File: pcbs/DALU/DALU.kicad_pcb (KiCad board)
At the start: 4 copper layers, 46 parts, among them J201 Conn_02x20_Odd_Even, U201 74HC245, U202 74HC245, U203 74HC245, U301 74HC138, U401 74HC86, U402 74HC86, U403 74HC86, U404 74HC08, U405 74HC283, U406 74HC283, U407 74HC245, U408 74HC245, U501 74HC00, U502 74HC00, U505 74HC245, U506 74HC245, U601 74HC86, U602 74HC86, U603 74HC245, U701 74HC245, U801 74HC74, U802 74HCT574

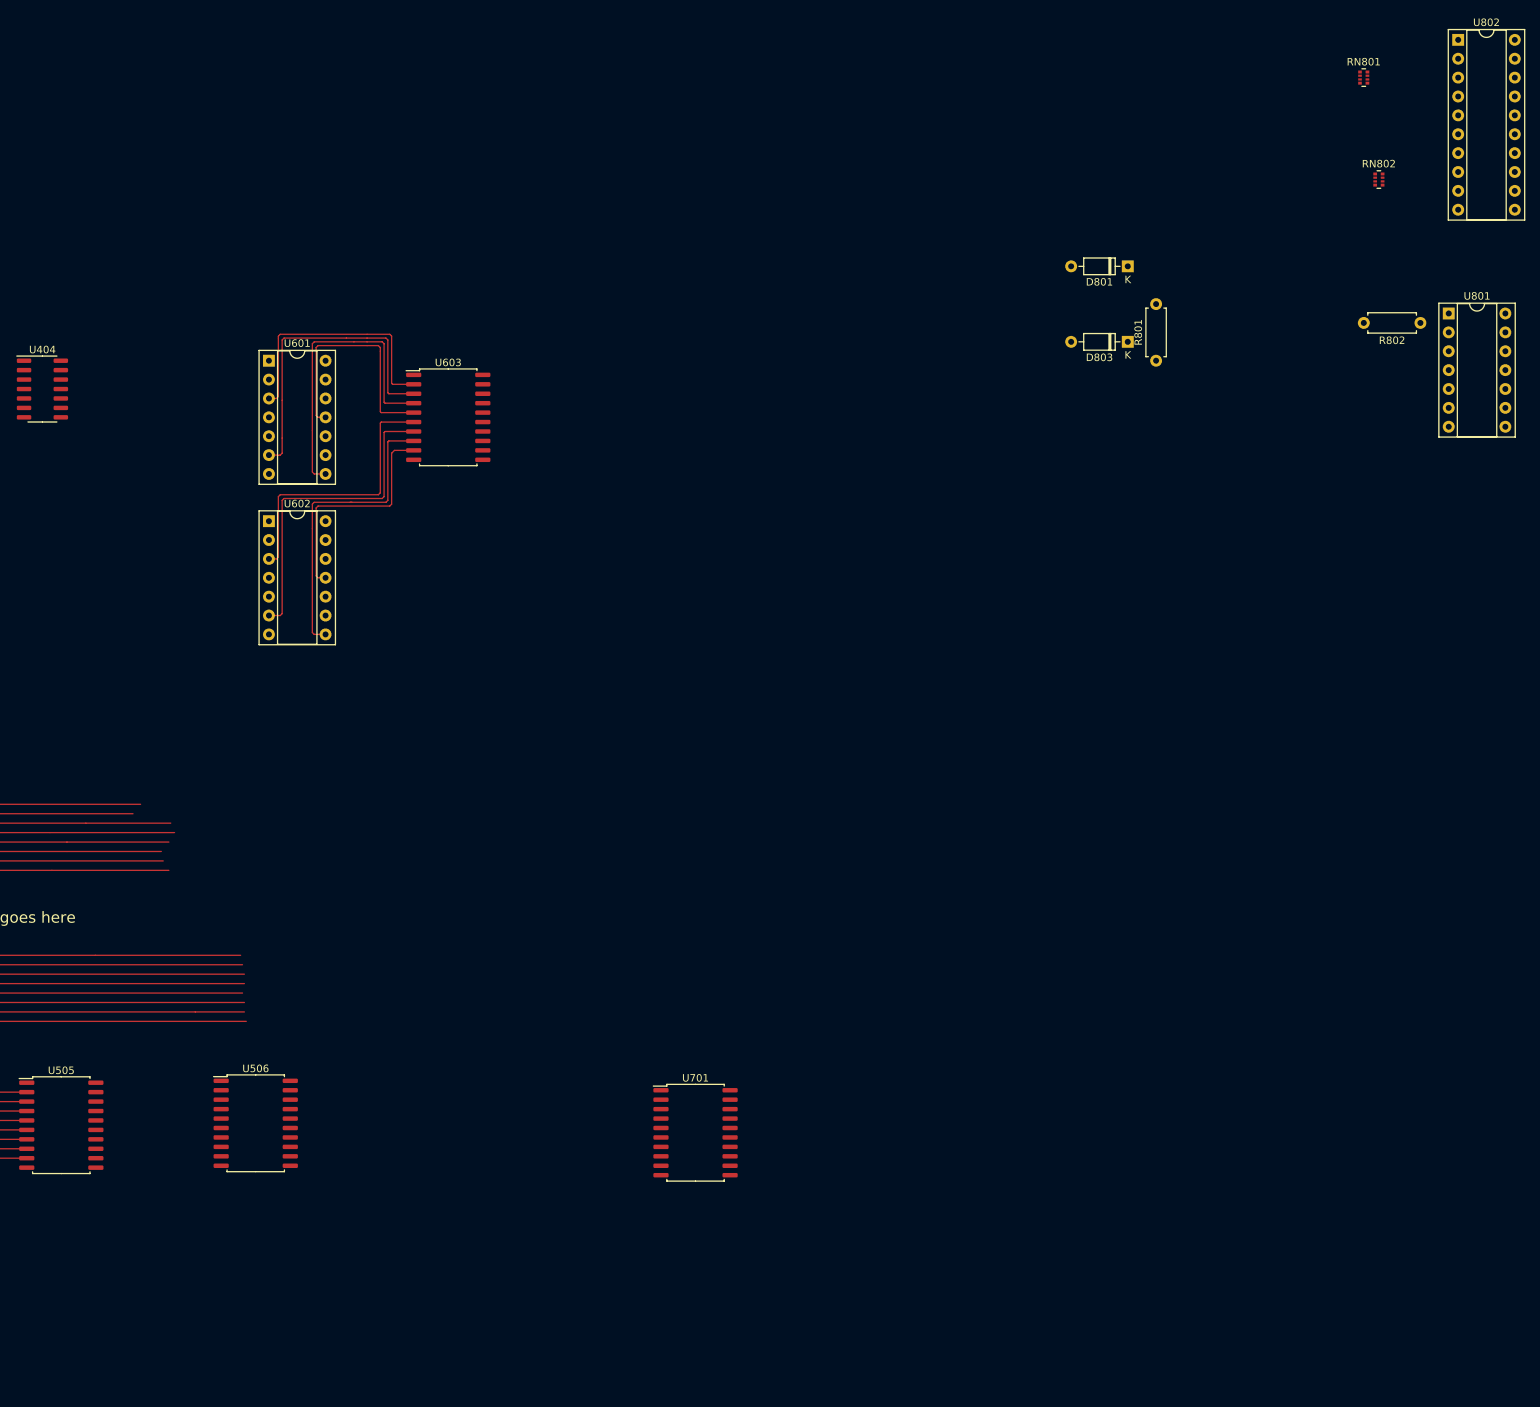
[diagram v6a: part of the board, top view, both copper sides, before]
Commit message: Separate out AND stage
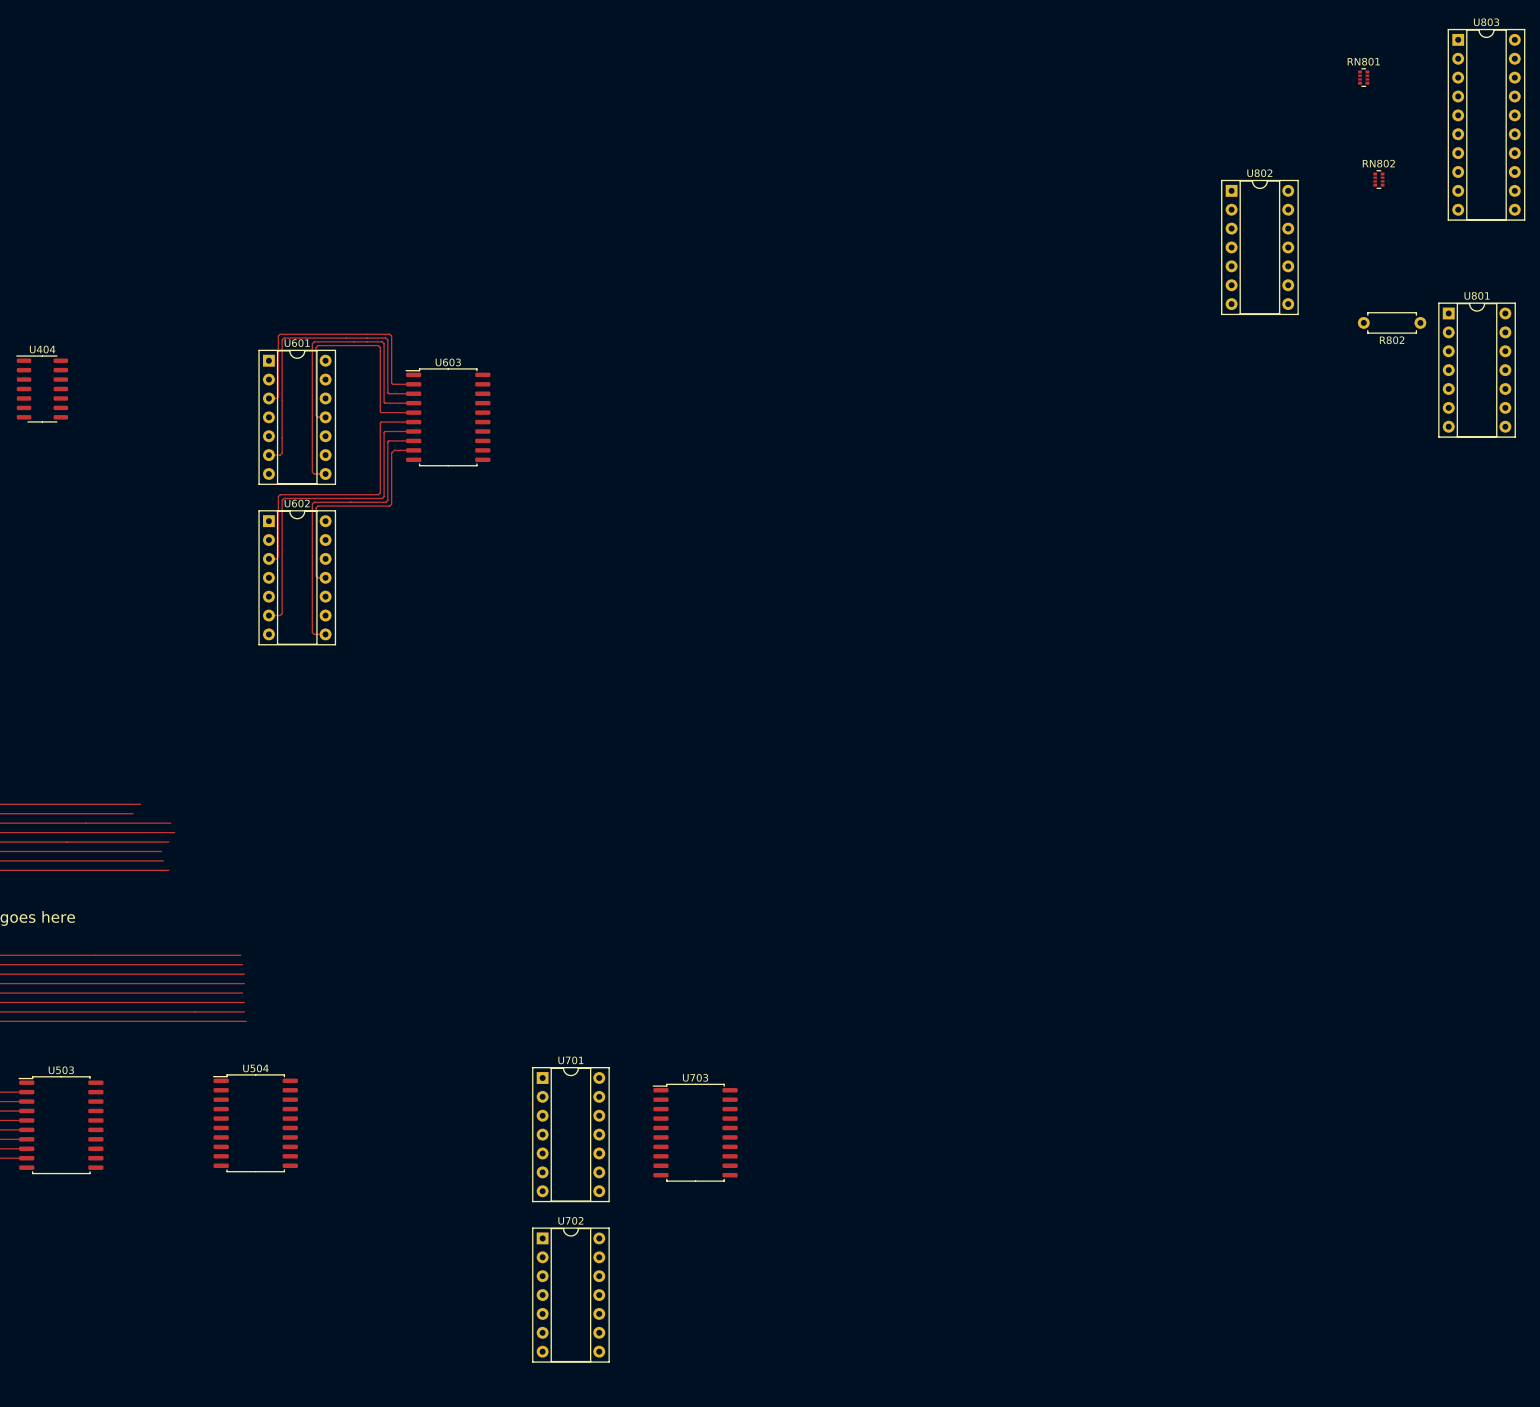
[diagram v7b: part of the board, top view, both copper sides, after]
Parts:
- removed D801, D803: 1N4148, Diode_THT:D_DO-35_SOD27_P7.62mm_Horizontal
- removed R801: 100k, Resistor_THT:R_Axial_DIN0207_L6.3mm_D2.5mm_P7.62mm_Horizontal
- added U701: 74HC32, Package_DIP:DIP-14_W7.62mm_Socket, F.Cu at (175.3, 143.5)
- added U702: 74HC32, Package_DIP:DIP-14_W7.62mm_Socket, F.Cu at (175.3, 165.1)
- added U802: 74HC32, Package_DIP:DIP-14_W7.62mm_Socket, F.Cu at (268.0, 24.1)
- renumbered U505 to U503, U506 to U504, U701 to U703, U802 to U803
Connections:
- U703 pad 2: unconnected-(U701-Pad2) -> /OR/OR0
- U703 pad 3: unconnected-(U701-Pad3) -> /OR/OR1
- U703 pad 4: unconnected-(U701-Pad4) -> /OR/OR2
- U703 pad 5: unconnected-(U701-Pad5) -> /OR/OR3
- U703 pad 6: unconnected-(U701-Pad6) -> /OR/OR4
- U703 pad 7: unconnected-(U701-Pad7) -> /OR/OR5
- U703 pad 8: unconnected-(U701-Pad8) -> /OR/OR6
- U703 pad 9: unconnected-(U701-Pad9) -> /OR/OR7

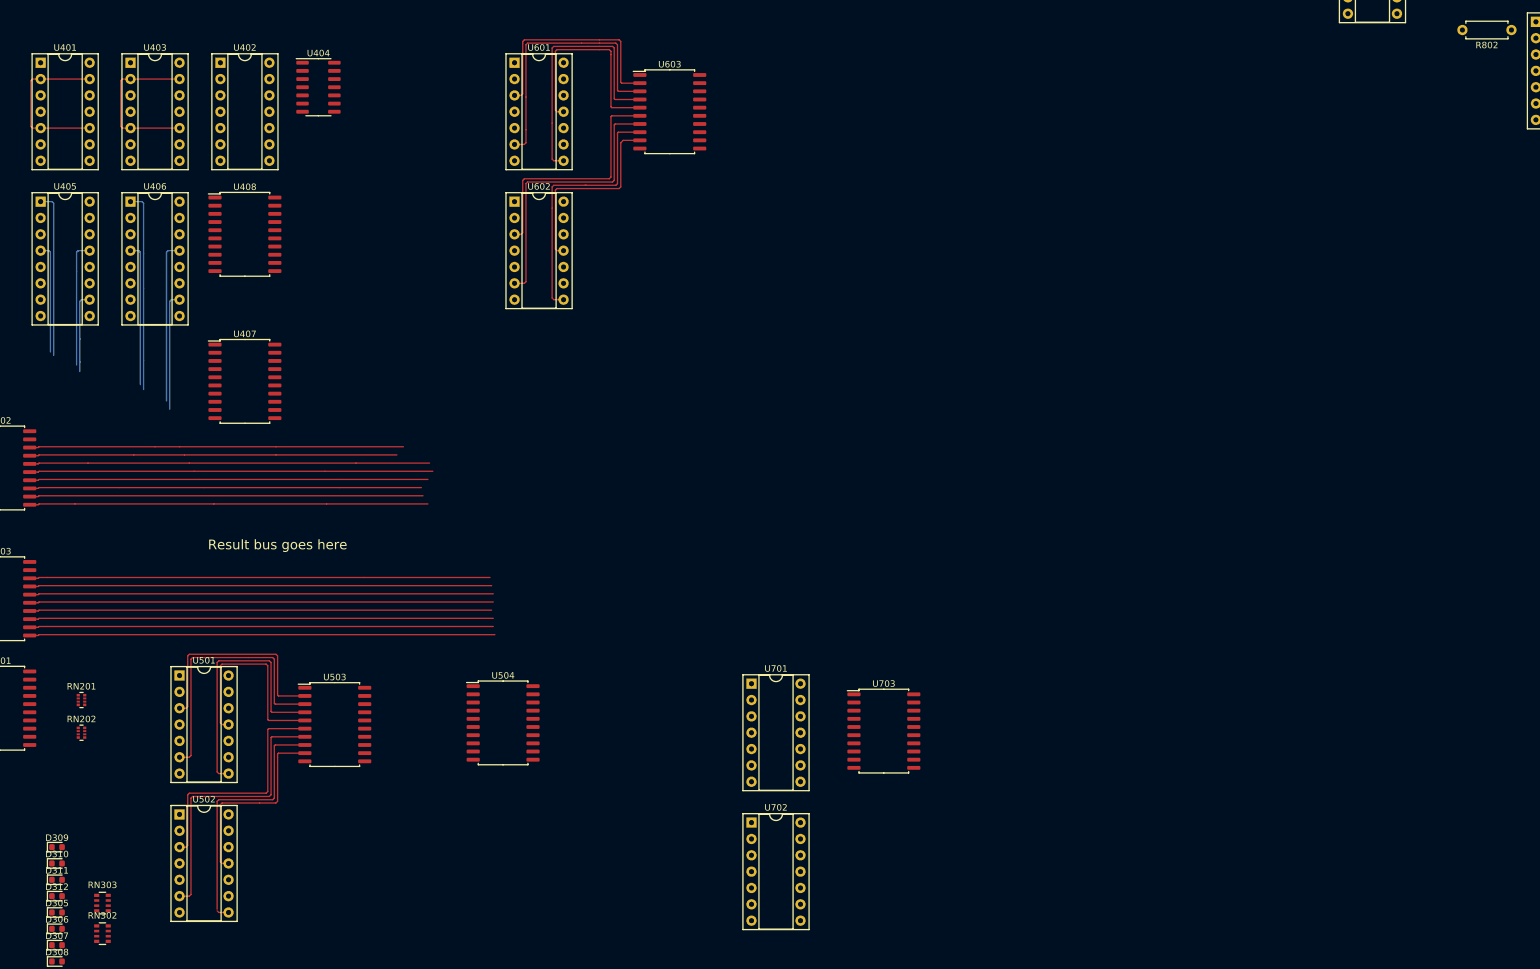
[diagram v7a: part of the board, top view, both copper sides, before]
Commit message: Routing.... have realised that I need to think more about vias
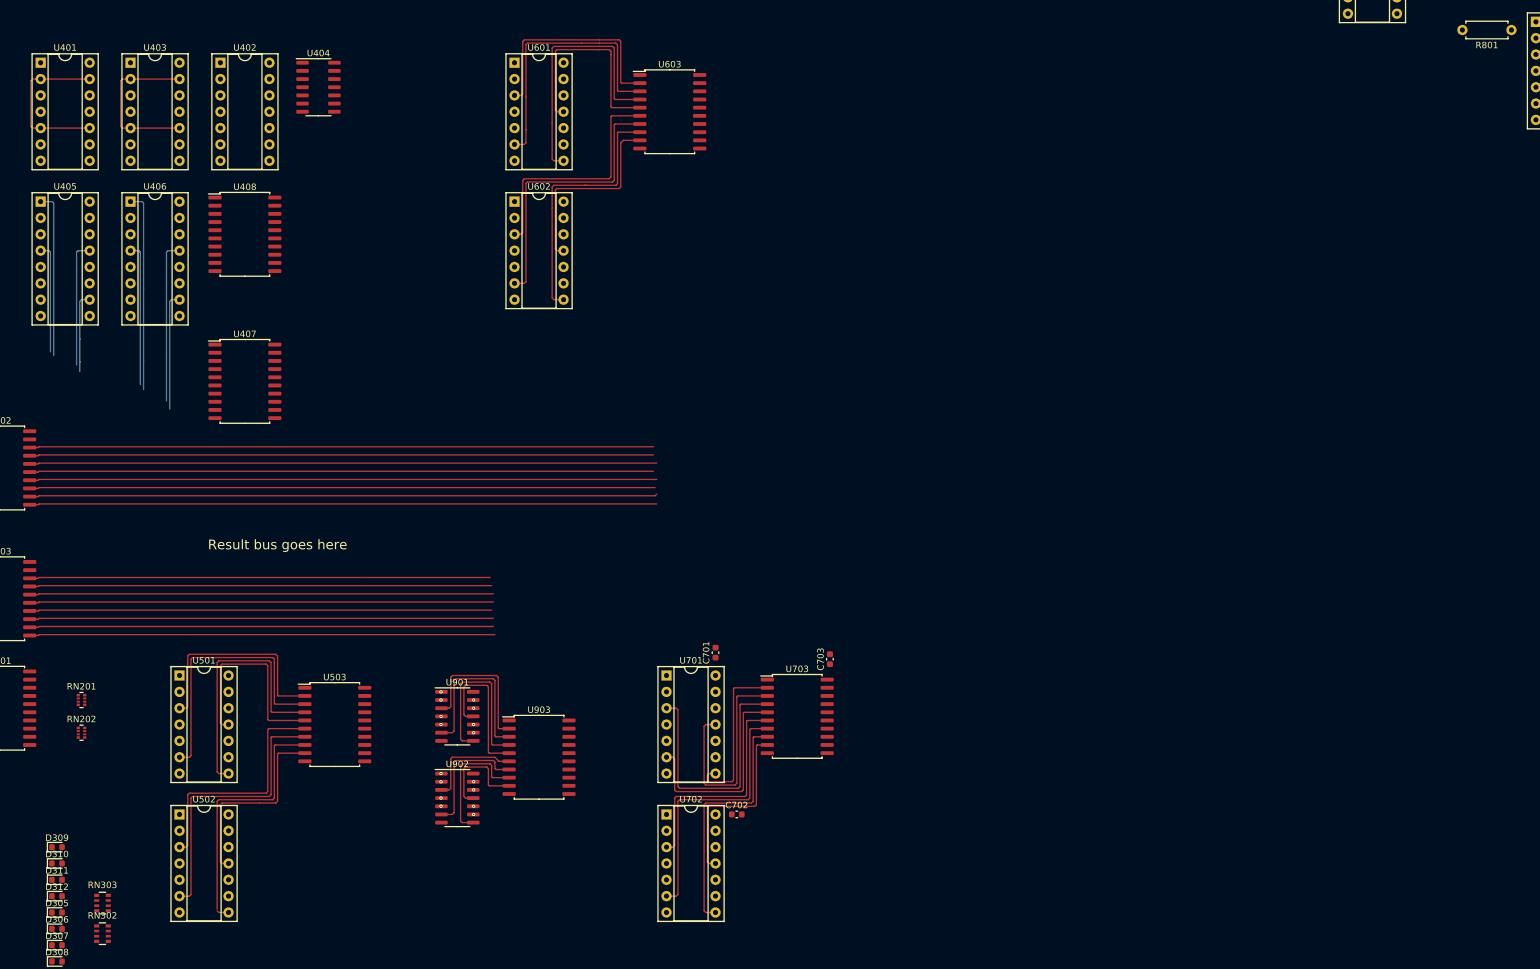
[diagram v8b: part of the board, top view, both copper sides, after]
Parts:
- removed U504: 74HC245, Package_SO:SOIC-20W_7.5x12.8mm_P1.27mm
- added C701: 100n, Capacitor_SMD:C_0603_1608Metric, F.Cu at (169.7, 138.7)
- added C702: 100n, Capacitor_SMD:C_0603_1608Metric, F.Cu at (173.0, 163.8)
- added C703: 100n, Capacitor_SMD:C_0603_1608Metric, F.Cu at (187.5, 139.7)
- added U901: 74HC08, Package_SO:SOIC-14_3.9x8.7mm_P1.27mm, F.Cu at (129.5, 148.6)
- added U902: 74HC08, Package_SO:SOIC-14_3.9x8.7mm_P1.27mm, F.Cu at (129.5, 161.3)
- added U903: 74HC245, Package_SO:SOIC-20W_7.5x12.8mm_P1.27mm, F.Cu at (142.2, 154.9)
- moved U703 13.7 mm to (182.4, 148.6)
- moved U701 13.3 mm to (162.1, 142.2)
- moved U702 13.3 mm to (162.1, 163.8)
- renumbered R802 to R801
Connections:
- net /AND-NAND/A4 renamed /AND/A4
- net /AND-NAND/A5 renamed /AND/A5
- net /AND-NAND/A6 renamed /AND/A6
- net /AND-NAND/A7 renamed /AND/A7
- net /AND-NAND/B4 renamed /AND/B4
- net /AND-NAND/B5 renamed /AND/B5
- net /AND-NAND/B6 renamed /AND/B6
- net /AND-NAND/B7 renamed /AND/B7
- net /AND-NAND/NAND0 renamed /NAND/NAND0
- net /AND-NAND/NAND1 renamed /NAND/NAND1
- net /AND-NAND/NAND2 renamed /NAND/NAND2
- net /AND-NAND/NAND3 renamed /NAND/NAND3
- net /AND-NAND/NAND4 renamed /NAND/NAND4
- net /AND-NAND/NAND5 renamed /NAND/NAND5
- net /AND-NAND/NAND6 renamed /NAND/NAND6
- net /AND-NAND/NAND7 renamed /NAND/NAND7
- net /AND-NAND/~{NAND} renamed /NAND/~{NAND}
- U202 pad 15: /AND-NAND/A3 -> /AND/A3
- U202 pad 16: /AND-NAND/A2 -> /AND/A2
- U202 pad 17: /AND-NAND/A1 -> /AND/A1
- U202 pad 18: /AND-NAND/A0 -> /AND/A0
- U203 pad 15: /AND-NAND/B3 -> /AND/B3
- U203 pad 16: /AND-NAND/B2 -> /AND/B2
- U203 pad 17: /AND-NAND/B1 -> /AND/B1
- U203 pad 18: /AND-NAND/B0 -> /AND/B0
- U401 pad 1: /AND-NAND/B0 -> /AND/B0
- U401 pad 12: /AND-NAND/B3 -> /AND/B3
- U401 pad 4: /AND-NAND/B1 -> /AND/B1
- U401 pad 9: /AND-NAND/B2 -> /AND/B2
- U405 pad 12: /AND-NAND/A3 -> /AND/A3
- U405 pad 14: /AND-NAND/A2 -> /AND/A2
- U405 pad 3: /AND-NAND/A1 -> /AND/A1
- U405 pad 5: /AND-NAND/A0 -> /AND/A0
- U501 pad 1: /AND-NAND/A0 -> /AND/A0
- U501 pad 10: /AND-NAND/B2 -> /AND/B2
- U501 pad 12: /AND-NAND/A3 -> /AND/A3
- U501 pad 13: /AND-NAND/B3 -> /AND/B3
- U501 pad 2: /AND-NAND/B0 -> /AND/B0
- U501 pad 4: /AND-NAND/A1 -> /AND/A1
- U501 pad 5: /AND-NAND/B1 -> /AND/B1
- U501 pad 9: /AND-NAND/A2 -> /AND/A2
- U503 pad 11: /AND-NAND/RESULT7 -> /NAND/RESULT7
- U503 pad 12: /AND-NAND/RESULT6 -> /NAND/RESULT6
- U503 pad 13: /AND-NAND/RESULT5 -> /NAND/RESULT5
- U503 pad 14: /AND-NAND/RESULT4 -> /NAND/RESULT4
- U503 pad 15: /AND-NAND/RESULT3 -> /NAND/RESULT3
- U503 pad 16: /AND-NAND/RESULT2 -> /NAND/RESULT2
- U503 pad 17: /AND-NAND/RESULT1 -> /NAND/RESULT1
- U503 pad 18: /AND-NAND/RESULT0 -> /NAND/RESULT0
- U601 pad 1: /AND-NAND/A0 -> /AND/A0
- U601 pad 10: /AND-NAND/B2 -> /AND/B2
- U601 pad 12: /AND-NAND/A3 -> /AND/A3
- U601 pad 13: /AND-NAND/B3 -> /AND/B3
- U601 pad 2: /AND-NAND/B0 -> /AND/B0
- U601 pad 4: /AND-NAND/A1 -> /AND/A1
- U601 pad 5: /AND-NAND/B1 -> /AND/B1
- U601 pad 9: /AND-NAND/A2 -> /AND/A2
- U701 pad 1: /AND-NAND/A0 -> /AND/A2
- U701 pad 10: /AND-NAND/B2 -> /AND/B0
- U701 pad 11: /OR/OR3 -> /OR/OR1
- U701 pad 12: /AND-NAND/A3 -> /AND/A1
- U701 pad 13: /AND-NAND/B3 -> /AND/B1
- U701 pad 14: unconnected-(U701-Pad14) -> +5V
- U701 pad 2: /AND-NAND/B0 -> /AND/B2
- U701 pad 3: /OR/OR0 -> /OR/OR2
- U701 pad 4: /AND-NAND/A1 -> /AND/A3
- U701 pad 5: /AND-NAND/B1 -> /AND/B3
- U701 pad 6: /OR/OR1 -> /OR/OR3
- U701 pad 7: unconnected-(U701-Pad7) -> GND
- U701 pad 8: /OR/OR2 -> /OR/OR0
- U701 pad 9: /AND-NAND/A2 -> /AND/A0
- U702 pad 14: unconnected-(U702-Pad14) -> +5V
- U702 pad 7: unconnected-(U702-Pad7) -> GND
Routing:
- net /AND/B0: track 0.00 -> 187.2 mm, vias 0 -> 1
- net /AND/B3: track 0.00 -> 182.4 mm, vias 0 -> 1
- net /AND/A1: track 0.00 -> 182.4 mm, vias 0 -> 1
- net /AND/A2: track 0.00 -> 181.3 mm, vias 0 -> 1
- net /AND/A0: track 0.00 -> 180.8 mm, vias 0 -> 1
- net /AND/A3: track 0.00 -> 177.8 mm, vias 0 -> 1
- net /AND/B1: track 0.00 -> 176.0 mm, vias 0 -> 1
- net /AND/B2: track 0.00 -> 170.4 mm, vias 0 -> 1
- net /AND-NAND/B0: track 167.7 -> 0.00 mm
- net /AND-NAND/B3: track 163.1 -> 0.00 mm
- net /AND-NAND/B1: track 160.6 -> 0.00 mm
- net /AND-NAND/B2: track 155.2 -> 0.00 mm
- net /AND-NAND/A2: track 131.4 -> 0.00 mm
- net /AND-NAND/A3: track 124.8 -> 0.00 mm
- net /AND-NAND/A1: track 124.8 -> 0.00 mm
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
